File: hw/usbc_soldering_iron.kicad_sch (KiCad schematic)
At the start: 77 parts, among them J1 U263-163N-4OS1735, J10 TIP_G, J11 TIP_R, J12 TIP_B, J13 TIP_G, J14 TIP_R, J15 TIP_B, J16 TIP_G, J2 DBG, J3 LED RING, J4 OLED, J5 TIP_R, J6 TIP_B, J7 TIP_G, J8 TIP_R, J9 TIP_B, Q1 AGM403AP, U1 CH32X035F8U6, U10 AP63203WU, U11 SIQ-02FVS3, U2 TPA191Ax, U3 TPD4E05U06DQA, U5 SC7A20, U6 MT3608, U7 TLV333IDBVR, U8 IRS20752L, IRS20752L, NSG10752

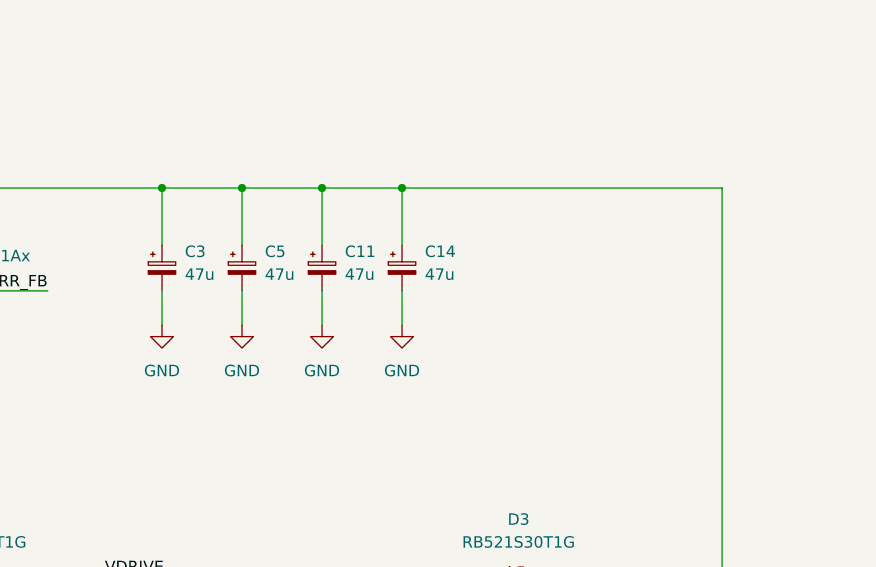
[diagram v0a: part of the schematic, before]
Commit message: different capacitors and new bom
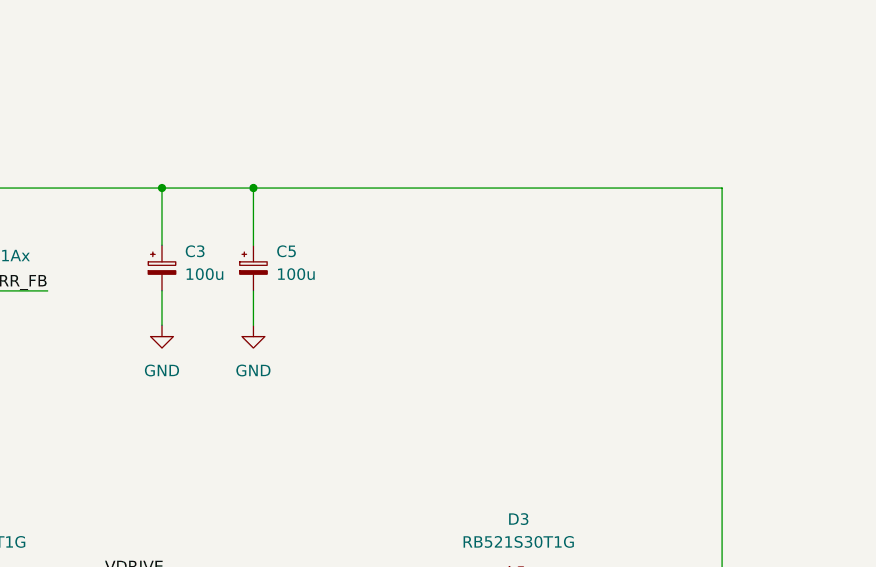
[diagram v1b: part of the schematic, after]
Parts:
- removed C11, C14: 47u, Custom:CPol_Circular_Bent_D5mm_L6mm, symbol Device:C_Polarized_Small
- C3: value 47u -> 100u; footprint Custom:CPol_Circular_Bent_D5mm_L6mm -> Custom:CPol_Circular_Bent_D6.3mm_L8mm_L
- C5: value 47u -> 100u; footprint Custom:CPol_Circular_Bent_D5mm_L6mm -> Custom:CPol_Circular_Bent_D6.3mm_L8mm_R
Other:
- moved on the sheet: C5

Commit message: new filter design, may work lmao
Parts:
- removed C5: 100u, Custom:CPol_Circular_Bent_D6.3mm_L8mm_R, symbol Device:C_Polarized_Small
- removed R25: 1k, Resistor_SMD:R_0603_1608Metric, symbol Device:R_Small
- added C11, C14, C21, C23, C5: 10u, Capacitor_SMD:C_1210_3225Metric, symbol Device:C_Small
- added L2: 2.2u, Inductor_SMD:L_Changjiang_FNR4030S, symbol Device:L
- C3: footprint Custom:CPol_Circular_Bent_D6.3mm_L8mm_L -> Custom:CP-SMD_L7.3-W4.3-FD
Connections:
- net GND: now also C11.2, C14.2, C21.2, C23.2, C5.2
- net TC_FB: now also C27.2, R24.2, U7.1
- net at C3.1, R10.2, U2.5 (IN-): now also C5.1, L2.1; no longer Q1.5 (D)
- new net VDRV: C11.1, C14.1, C21.1, C23.1, L2.2, Q1.5 (D)
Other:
- moved on the sheet: C29, C3, C7, C8, D1, D2, D3, D4, L3, Q1, R10, R19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

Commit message: some component changes
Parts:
- removed D4: 3.3V, Diode_SMD:D_SOD-523, symbol Device:D_Zener_Small
- removed J3: LED RING, Connector_PinHeader_1.27mm:PinHeader_1x03_P1.27mm_Vertical, symbol Connector:Conn_01x03_Socket
- removed R6: 100k, Resistor_SMD:R_0603_1608Metric, symbol Device:R_Small
- removed R8: 10k, Resistor_SMD:R_0603_1608Metric, symbol Device:R_Small
- removed U2: TPA191Ax, Package_TO_SOT_SMD:SOT-363_SC-70-6, symbol custom_library:TPA191Ax
- added U7: INA226, Package_SO:VSSOP-10_3x3mm_P0.5mm, symbol Sensor_Energy:INA226
- R11: renamed from R10; value 1.5m -> 2m
- renumbered C27 to C10, C12 to C11, C7 to C12, C3 to C13, C15 to C14, C5 to C15, C11 to C19, C19 to C20, C14 to C21, C20 to C22, C21 to C23, C23 to C24, C8 to C25, C29 to C26, C13 to C3, C22 to C4, C6 to C5, C9 to C6, C10 to C7, C24 to C8, C4 to C9, D6 to D1, D5 to D2, D1 to D3, D3 to D4, D2 to D5, J11 to J10, J12 to J11, J13 to J12, J14 to J13, J15 to J14, J16 to J15, J4 to J3, J5 to J4, J6 to J5, J7 to J6, J8 to J7, J9 to J8, J10 to J9, R24 to R10, R19 to R14, R21 to R15, R11 to R6, R15 to R8, R20 to R9, U5 to U1, U1 to U2, U11 to U4, U10 to U5, U7 to U6, U6 to U8, U8 to U9
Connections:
- net +3.3V: now also U1.10 (~{CS}), U7.6 (VS); no longer U1.11 (NC)
- net GND: now also U7.1 (A1), U7.2 (A0), U7.7 (GND)
- net SCL: now also U7.5 (SCL)
- net SDA: now also U7.4 (SDA)
- net VBUS: now also U7.10 (Vin+), U7.8 (Vbus)
- net at C13.1, C15.1, L2.1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: now also U7.9 (Vin-)
- net POW_ALERT: now reaches U2.15 (PB12)
- net POW_ALERT: now also U7.3 (~{Alert})
- net CURR_FB: no longer names the net of U2.4 (PA2)
- net LED_RING: no longer names the net of U2.10 (PB0)
- no-connect marks 10 -> 13
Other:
- note removed: "LED RING"
- moved on the sheet: C10, C12, C23, C24, C3, C4, C6, C8, D2, D4, R10, R6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

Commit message: boxed version
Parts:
- removed J10, J13, J4, J7: TIP_R, Connector_Wire:SolderWire-0.25sqmm_1x01_D0.65mm_OD1.7mm, symbol Connector_Generic:Conn_01x01
- removed J11, J14, J5, J8: TIP_B, Connector_Wire:SolderWire-0.25sqmm_1x01_D0.65mm_OD1.7mm, symbol Connector_Generic:Conn_01x01
- removed J12, J15, J6, J9: TIP_G, Connector_Wire:SolderWire-0.25sqmm_1x01_D0.65mm_OD1.7mm, symbol Connector_Generic:Conn_01x01
- added H1, H2, H3, H4: MountingHole, MountingHole:MountingHole_2.2mm_M2_DIN965, symbol Mechanical:MountingHole
- added J16: TIP_CONN, TerminalBlock_Phoenix:TerminalBlock_Phoenix_MKDS-1,5-3_1x03_P5.00mm_Horizontal, symbol Connector:Screw_Terminal_01x03
- added J4: GPIO, Connector_PinHeader_2.54mm:PinHeader_1x04_P2.54mm_Vertical, symbol Connector:Conn_01x04_Pin
- added J5: DISP, Connector_PinSocket_2.54mm:PinSocket_1x04_P2.54mm_Vertical, symbol Connector:Conn_01x04_Socket
- J2: footprint Connector_PinHeader_1.27mm:PinHeader_1x04_P1.27mm_Vertical -> Connector_PinHeader_2.54mm:PinHeader_1x04_P2.54mm_Vertical; symbol Connector:Conn_01x04_Socket -> Connector:Conn_01x04_Pin
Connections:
- net +3.3V: now also J5.3 (Pin_3)
- net BLUE: now also J16.2 (Pin_2)
- net GND: now also J16.3 (Pin_3), J5.4 (Pin_4)
- net RED: now also J16.1 (Pin_1)
- net SCL: now also J5.2 (Pin_2)
- net SDA: now also J5.1 (Pin_1)
- net PB0: now reaches U2.10 (PB0)
- net PB0: now also J4.4 (Pin_4)
- net PA2: now reaches U2.4 (PA2)
- net PA2: now also J4.1 (Pin_1)
- net PA3: now reaches U2.5 (PA3)
- net PA3: now also J4.2 (Pin_2)
- net PA4: now reaches U2.6 (PA4)
- net PA4: now also J4.3 (Pin_3)
- no-connect marks 13 -> 9

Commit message: test pads
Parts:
- added TP1: VBUS, TestPoint:TestPoint_Pad_D1.5mm, symbol Connector:TestPoint
- added TP2: GND, TestPoint:TestPoint_Pad_D1.5mm, symbol Connector:TestPoint
- added TP3: TIP, TestPoint:TestPoint_Pad_D1.5mm, symbol Connector:TestPoint
- added TP4: DRIVE, TestPoint:TestPoint_Pad_D1.5mm, symbol Connector:TestPoint
- added TP5: GATE, TestPoint:TestPoint_Pad_D1.5mm, symbol Connector:TestPoint
- added TP6: TC, TestPoint:TestPoint_Pad_D1.5mm, symbol Connector:TestPoint
- added TP7: NTC, TestPoint:TestPoint_Pad_D1.5mm, symbol Connector:TestPoint
- added TP8: 3V3, TestPoint:TestPoint_Pad_D1.5mm, symbol Connector:TestPoint
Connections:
- net +3.3V: now also TP8.1
- net GND: now also TP2.1
- net NTC: now also TP7.1
- net TC_FB: now also TP6.1
- net VBUS: now also TP1.1
- net VDRIVE: now also TP4.1
- net at Q1.4 (G), U9.5 (HO): now also TP5.1
- net VDRV renamed VTIP
- net VTIP: now also TP3.1
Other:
- moved on the sheet: C10, C8, D2, R10, R8, R9, U6

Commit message: finished pcb
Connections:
- net CC1: now also U3.2 (D1-); no longer U3.5 (D2-)
- net JDP: now also U3.5 (D2-); no longer U3.2 (D1-)
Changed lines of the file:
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@@
+		)
+	)
+	(label "JDN"
+		(at 76.2 71.12 180)
+		(effects
+			(font
+				(size 1.27 1.27)
+			)
+			(justify right bottom)
 		)
 	)
@@
 		)
 	)
+	(label "JDP"
+		(at 76.2 76.2 180)
+		(effects
+			(font
+				(size 1.27 1.27)
+			)
+			(justify right bottom)
+		)
+	)
 	(label "HEATER_ON"
 		(at 69.85 153.67 180)
@@
 		)
 	)
-	(label "JDN"
-		(at 76.2 71.12 180)
-		(effects
-			(font
-				(size 1.27 1.27)
-			)
-			(justify right bottom)
-		)
-	)
 	(label "VTIP"
 		(at 379.73 181.61 180)
@@
 		)
 	)
-	(label "JDP"
-		(at 41.91 76.2 0)
-		(effects
-			(font
-				(size 1.27 1.27)
-			)
-			(justify left bottom)
-		)
-	)
 	(label "TC_FB"
 		(at 69.85 140.97 180)
@@
 	)
 	(label "CC1"
-		(at 76.2 76.2 180)
-		(effects
-			(font
-				(size 1.27 1.27)
-			)
-			(justify right bottom)
-		)
-	)
+		(at 41.91 76.2 0)
+		(effects
+			(font
+				(size 1.27 1.27)
+			)
+			(justify left bottom)
+		)
+	)

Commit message: silkscreen
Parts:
- removed TP2: GND, TestPoint:TestPoint_Pad_D1.5mm, symbol Connector:TestPoint
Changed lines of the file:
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@@
 	)
 	(symbol
-		(lib_id "power:GND")
-		(at 40.64 95.25 0)
-		(unit 1)
-		(exclude_from_sim no)
-		(in_bom yes)
-		(on_board yes)
-		(dnp no)
-		(fields_autoplaced yes)
-		(property "Reference" "#PWR059"
-			(at 40.64 101.6 0)
-			(effects
-				(font
-					(size 1.27 1.27)
-				)
-				(hide yes)
-			)
-		)
-		(property "Value" "GND"
-			(at 40.64 100.33 0)
-			(effects
-				(font
-					(size 1.27 1.27)
-				)
-			)
-		)
-		(property "Footprint" ""
-			(at 40.64 95.25 0)
-			(effects
-				(font
-					(size 1.27 1.27)
-				)
-				(hide yes)
-			)
-		)
-		(property "Datasheet" ""
-			(at 40.64 95.25 0)
-			(effects
-				(font
-					(size 1.27 1.27)
-				)
-				(hide yes)
-			)
-		)
-		(property "Description" "Power symbol creates a global label with name \"GND\" , ground"
-			(at 40.64 95.25 0)
-			(effects
-				(font
-					(size 1.27 1.27)
-				)
-				(hide yes)
-			)
-		)
-		(pin "1"
-		)
-		(instances
-			(project "usbc_soldering_iron"
-				(path "/7095b018-eac3-4b01-b374-28e3216c4fd8"
-					(reference "#PWR059")
-					(unit 1)
-				)
-			)
-		)
-	)
-	(symbol
 		(lib_id "Device:C_Small")
 		(at 231.14 123.19 0)
@@
 					(unit 1)
 				)
-			)
-		)
-	)
-	(symbol
-		(lib_id "Connector:TestPoint")
-		(at 40.64 95.25 0)
-		(unit 1)
-		(exclude_from_sim no)
-		(in_bom yes)
-		(on_board yes)
-		(dnp no)
-		(fields_autoplaced yes)
-		(property "Reference" "TP2"
-			(at 43.18 90.6779 0)
-			(effects
-				(font
-					(size 1.27 1.27)
-				)
-				(justify left)
-			)
-		)
-		(property "Value" "GND"
-			(at 43.18 93.2179 0)
-			(effects
-				(font
-					(size 1.27 1.27)
-				)
-				(justify left)
-			)
-		)
-		(property "Footprint" "TestPoint:TestPoint_Pad_D1.5mm"
-			(at 45.72 95.25 0)
-			(effects
-				(font
-					(size 1.27 1.27)
-				)
-				(hide yes)
-			)
-		)
-		(property "Datasheet" "~"
-			(at 45.72 95.25 0)
-			(effects
-				(font
-					(size 1.27 1.27)
-				)
-				(hide yes)
-			)
-		)
-		(property "Description" "test point"
-			(at 40.64 95.25 0)
-			(effects
-				(font
-					(size 1.27 1.27)
-				)
-				(hide yes)
-			)
-		)
-		(pin "1"
-		)
-		(instances
-			(project "usbc_soldering_iron"
-				(path "/7095b018-eac3-4b01-b374-28e3216c4fd8"
-					(reference "TP2")
-					(unit 1)
-				)

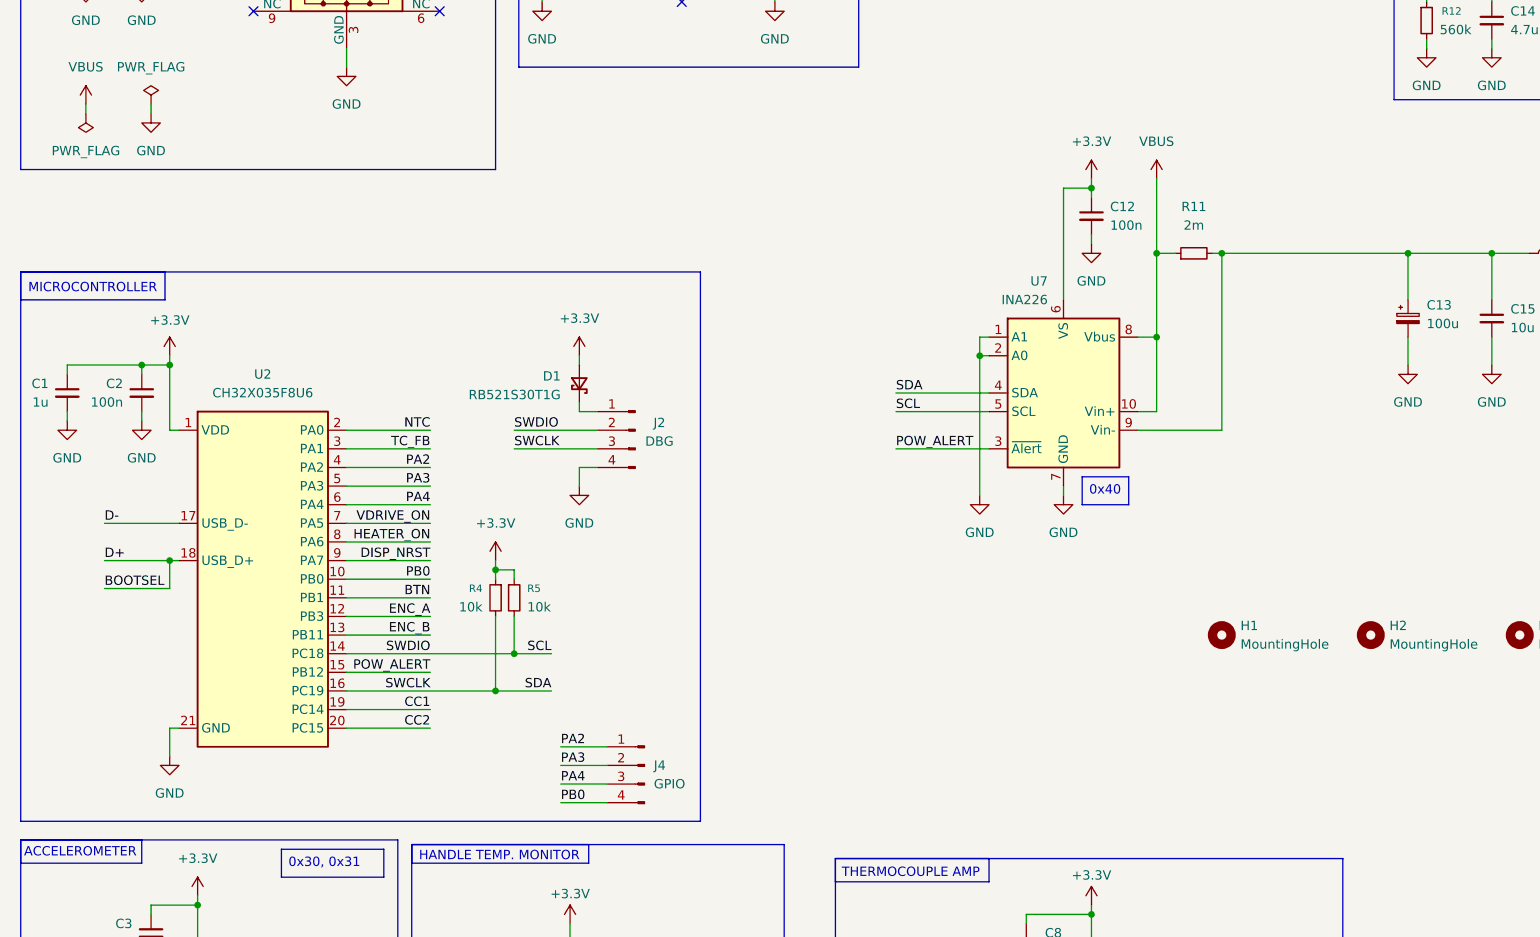
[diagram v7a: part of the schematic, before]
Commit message: different current sensor
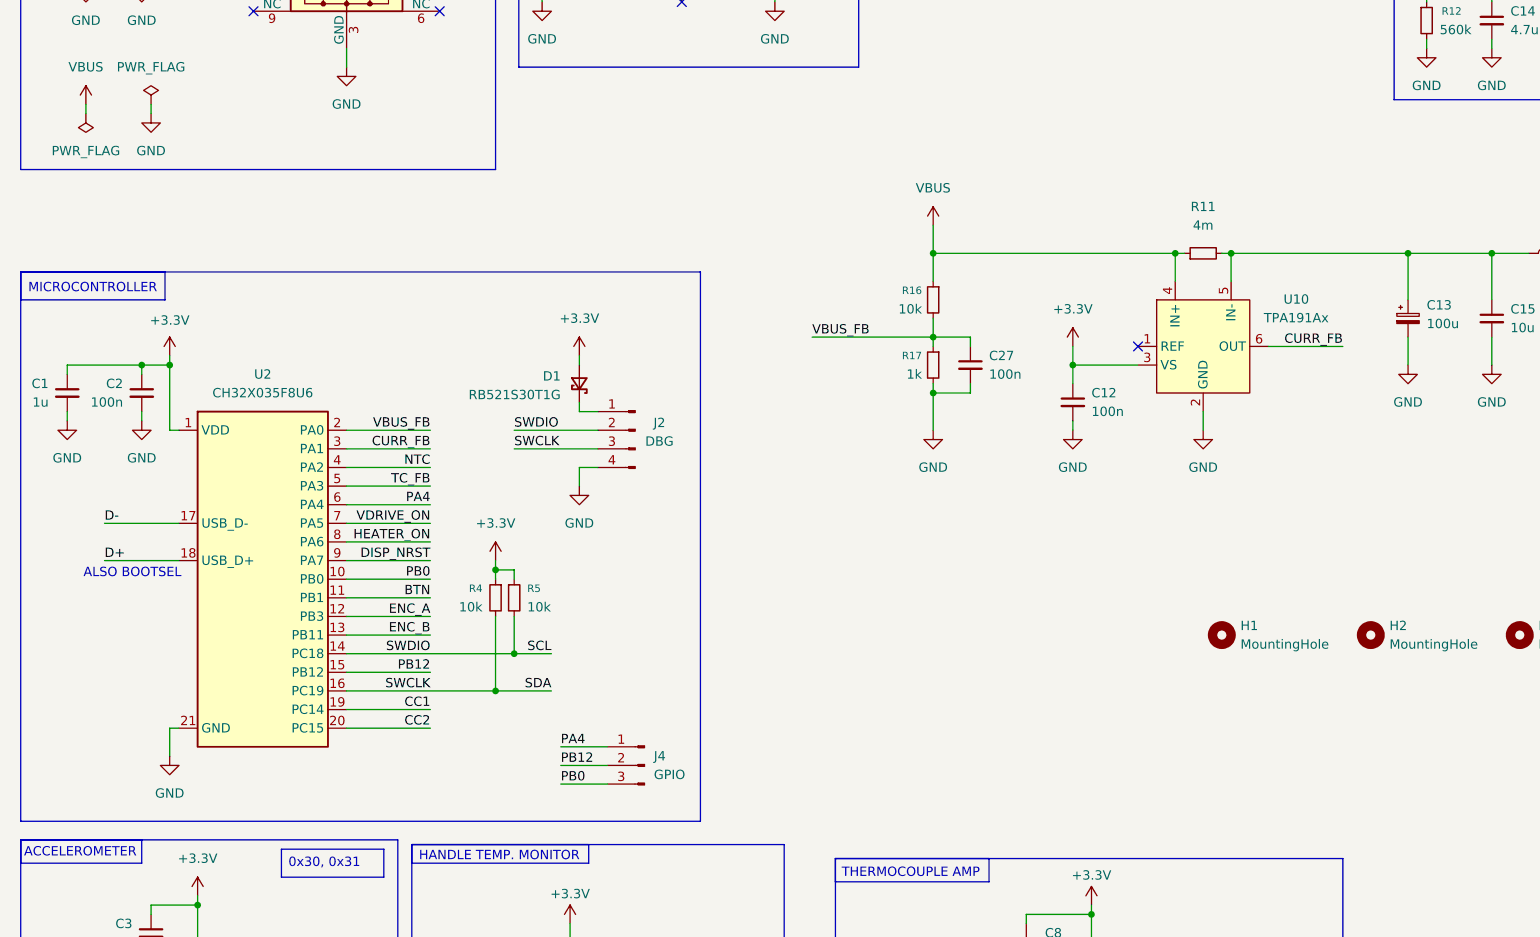
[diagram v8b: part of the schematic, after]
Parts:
- removed U7: INA226, Package_SO:VSSOP-10_3x3mm_P0.5mm, symbol Sensor_Energy:INA226
- added C27: 100n, Capacitor_SMD:C_0603_1608Metric, symbol Device:C_Small
- added R16: 10k, Resistor_SMD:R_0603_1608Metric, symbol Device:R_Small
- added R17: 1k, Resistor_SMD:R_0603_1608Metric, symbol Device:R_Small
- added U10: TPA191Ax, Package_TO_SOT_SMD:SOT-363_SC-70-6, symbol custom_library:TPA191Ax
- J4: footprint Connector_PinHeader_2.54mm:PinHeader_1x04_P2.54mm_Vertical -> Connector_PinHeader_2.54mm:PinHeader_1x03_P2.54mm_Vertical; symbol Connector:Conn_01x04_Pin -> Connector:Conn_01x03_Pin
- R11: value 2m -> 4m
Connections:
- net POW_ALERT is gone; now on net PB12: U2.15 (PB12)
- net +3.3V: now also U10.3 (VS)
- net GND: now also C27.2, R17.2, U10.2 (GND)
- net NTC: now also U2.4 (PA2); no longer U2.2 (PA0)
- net PA4: now also J4.1 (Pin_1); no longer J4.3 (Pin_3)
- net PB0: now also J4.3 (Pin_3); no longer J4.4 (Pin_4)
- net TC_FB: now also U2.5 (PA3); no longer U2.3 (PA1)
- net VBUS: now also R16.1, U10.4 (IN+)
- net at C13.1, C15.1, L2.1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: now also U10.5 (IN-)
- net BOOTSEL renamed D+
- removed net PA2: J4.1 (Pin_1), U2.4 (PA2)
- net PA3 renamed PB12
- net PB12: no longer U2.5 (PA3)
- new net CURR_FB: U10.6 (OUT), U2.3 (PA1)
- new net VBUS_FB: C27.1, R16.2, R17.1, U2.2 (PA0)
- no-connect marks 9 -> 10
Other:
- note added: "ALSO BOOTSEL"
- moved on the sheet: C12, R11
